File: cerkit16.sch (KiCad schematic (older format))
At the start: 33 parts, among them U1 ProMicro

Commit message: updated PCB
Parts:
- added RST1, RST2: TestPoint_Small, TestPoint:TestPoint_Pad_1.5x1.5mm, symbol Connector:TestPoint_Small
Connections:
- net GND: now also RST1.1
- net RST: now also RST2.1
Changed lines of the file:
@@
 	6550 1150 6400 1150
 $Comp
-L power:GND #PWR?
+L power:GND #PWR01
 U 1 1 5ED4B4E1
 P 6900 1100
-F 0 "#PWR?" H 6900 850 50  0001 C CNN
+F 0 "#PWR01" H 6900 850 50  0001 C CNN
 F 1 "GND" H 6905 927 50  0000 C CNN
 F 2 "" H 6900 1100 50  0001 C CNN
@@
 	6400 1050 6900 1050
 $Comp
-L power:GND #PWR?
+L power:GND #PWR02
 U 1 1 5ED4EA4A
 P 4750 1300
-F 0 "#PWR?" H 4750 1050 50  0001 C CNN
+F 0 "#PWR02" H 4750 1050 50  0001 C CNN
 F 1 "GND" H 4755 1127 50  0000 C CNN
 F 2 "" H 4750 1300 50  0001 C CNN
@@
 	4750 1150 4750 1250
 Connection ~ 4750 1250
+Wire Wire Line
+	4550 1250 4750 1250
+Text GLabel 3850 1500 0    50   Input ~ 0
+RST
+$Comp
+L Connector:TestPoint_Small RST2
+U 1 1 5ED6491C
+P 4000 1500
+F 0 "RST2" H 4048 1500 50  0000 L CNN
+F 1 "TestPoint_Small" H 4048 1455 50  0001 L CNN
+F 2 "TestPoint:TestPoint_Pad_1.5x1.5mm" H 4200 1500 50  0001 C CNN
+F 3 "~" H 4200 1500 50  0001 C CNN
+	1    4000 1500
+	1    0    0    -1
+$EndComp
+$Comp
+L Connector:TestPoint_Small RST1
+U 1 1 5ED5480B
+P 4550 1250
+F 0 "RST1" H 4500 1350 50  0000 L CNN
+F 1 "TestPoint_Small" H 4050 1150 50  0001 L CNN
+F 2 "TestPoint:TestPoint_Pad_1.5x1.5mm" H 4750 1250 50  0001 C CNN
+F 3 "~" H 4750 1250 50  0001 C CNN
+	1    4550 1250
+	1    0    0    -1
+$EndComp
+Wire Wire Line
+	4000 1500 3850 1500
 $EndSCHEMATC

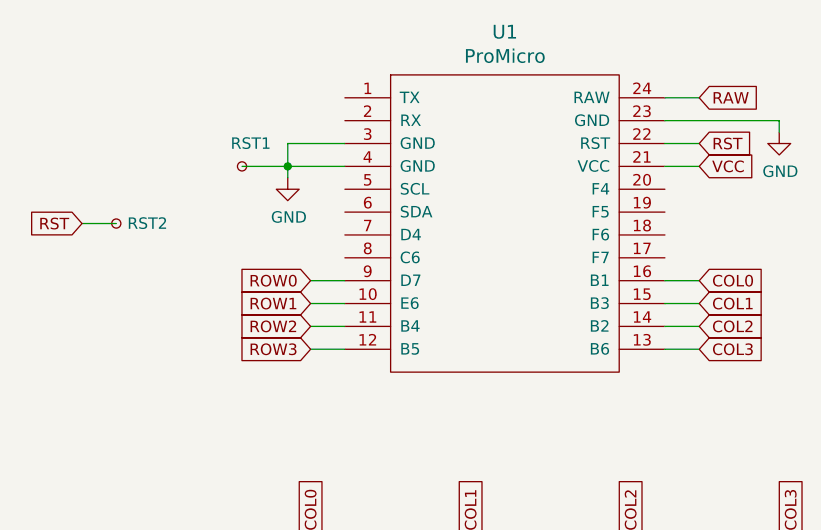
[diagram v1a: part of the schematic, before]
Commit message: moved the controller to the top of the board
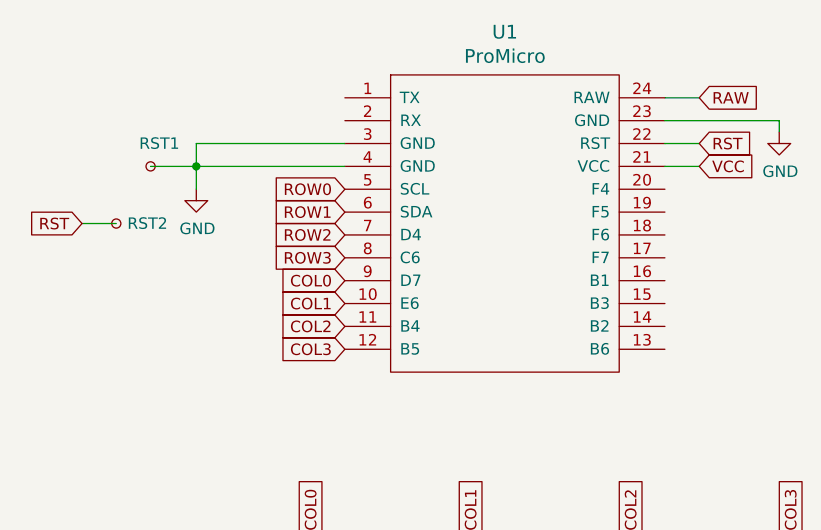
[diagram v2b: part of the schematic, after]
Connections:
- net COL0: now also U1.9 (D7); no longer U1.16 (B1)
- net COL1: now also U1.10 (E6); no longer U1.15 (B3)
- net COL2: now also U1.11 (B4); no longer U1.14 (B2)
- net COL3: now also U1.12 (B5); no longer U1.13 (B6)
- net ROW0: now also U1.5 (SCL); no longer U1.9 (D7)
- net ROW1: now also U1.6 (SDA); no longer U1.10 (E6)
- net ROW2: now also U1.7 (D4); no longer U1.11 (B4)
- net ROW3: now also U1.8 (C6); no longer U1.12 (B5)
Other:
- moved on the sheet: RST1
